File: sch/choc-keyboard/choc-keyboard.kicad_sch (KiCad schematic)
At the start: 1 part

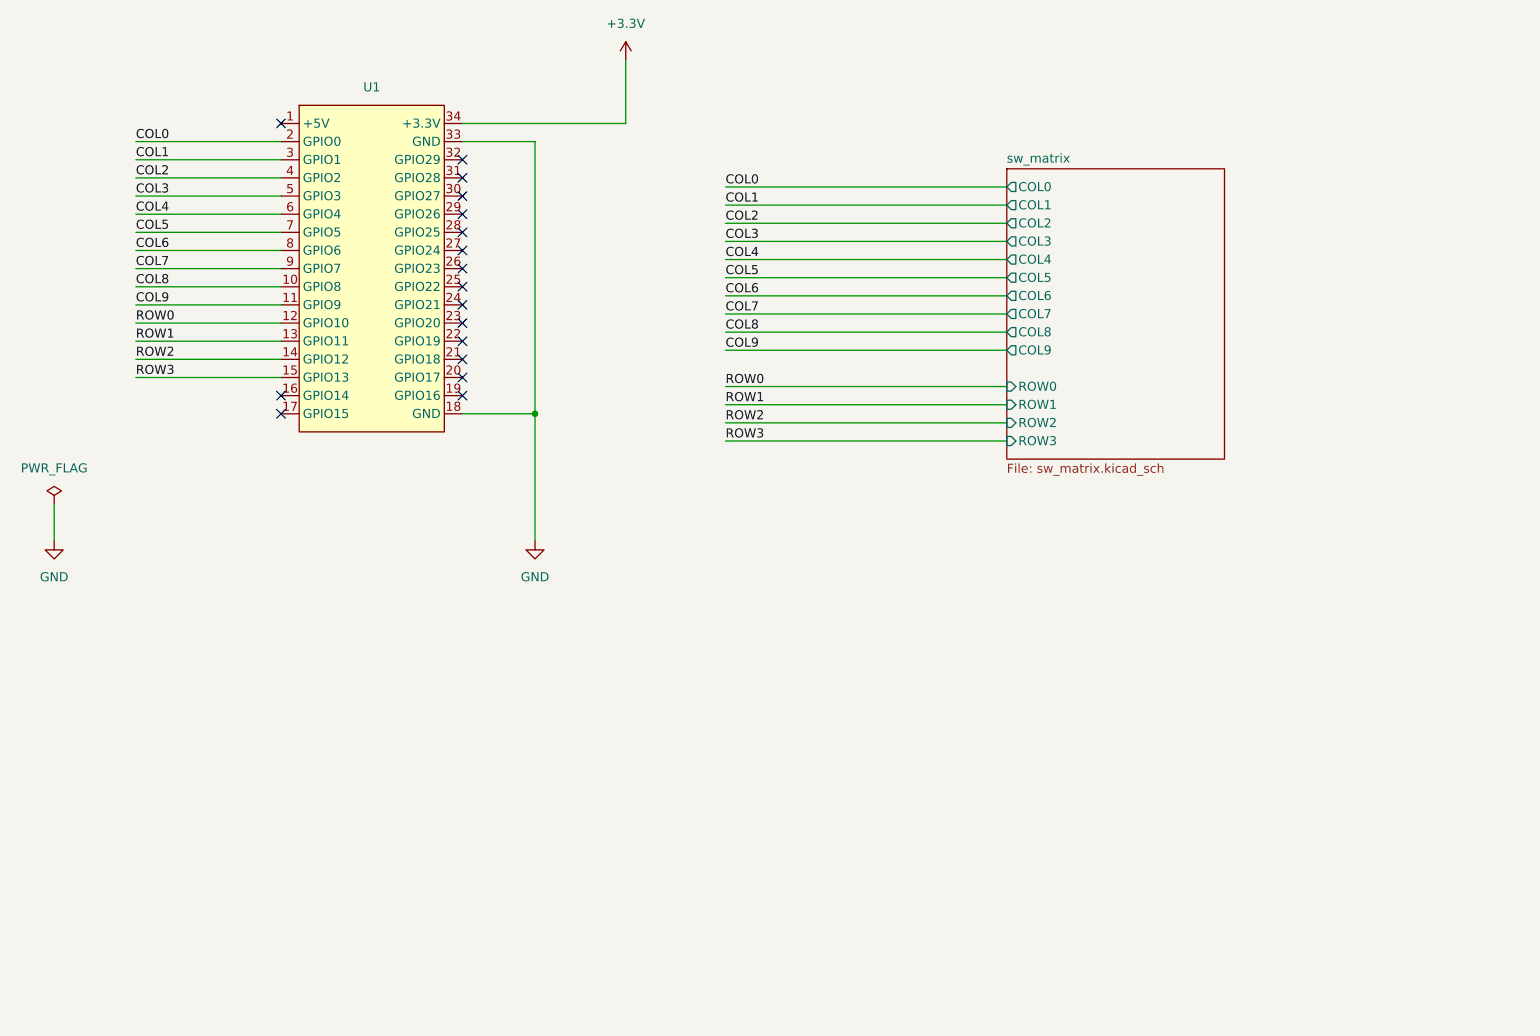
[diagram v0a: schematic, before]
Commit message: 配線しながらマイコンのピン配を検討中。
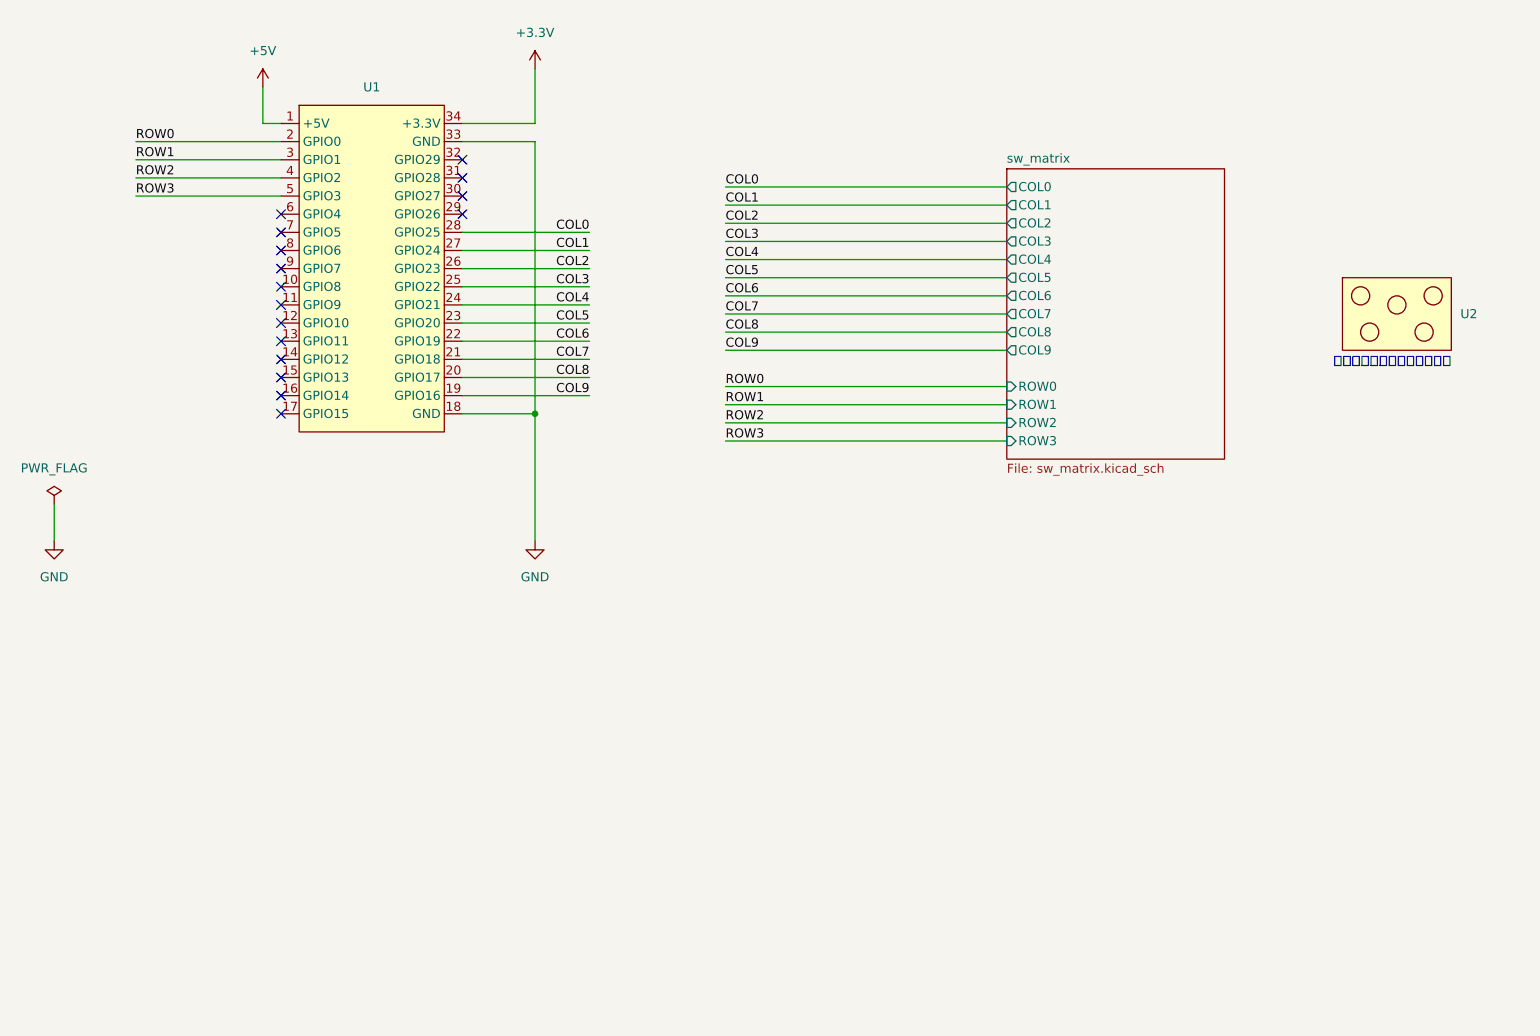
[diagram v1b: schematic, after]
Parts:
- added U2: ~, trackpoint:trackpoint_t400, symbol trackpoint:trackpoint_t400
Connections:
- net COL0: now also U1.28 (GPIO25); no longer U1.2 (GPIO0)
- net COL1: now also U1.27 (GPIO24); no longer U1.3 (GPIO1)
- net COL2: now also U1.26 (GPIO23); no longer U1.4 (GPIO2)
- net COL3: now also U1.25 (GPIO22); no longer U1.5 (GPIO3)
- net COL4: now also U1.24 (GPIO21); no longer U1.6 (GPIO4)
- net COL5: now also U1.23 (GPIO20); no longer U1.7 (GPIO5)
- net COL6: now also U1.22 (GPIO19); no longer U1.8 (GPIO6)
- net COL7: now also U1.21 (GPIO18); no longer U1.9 (GPIO7)
- net COL8: now also U1.20 (GPIO17); no longer U1.10 (GPIO8)
- net COL9: now also U1.19 (GPIO16); no longer U1.11 (GPIO9)
- net ROW0: now also U1.2 (GPIO0); no longer U1.12 (GPIO10)
- net ROW1: now also U1.3 (GPIO1); no longer U1.13 (GPIO11)
- net ROW2: now also U1.4 (GPIO2); no longer U1.14 (GPIO12)
- net ROW3: now also U1.5 (GPIO3); no longer U1.15 (GPIO13)
- net +5V: now reaches U1.1 (+5V)
- no-connect marks 17 -> 16
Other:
- note added: "トラックポイント取り付け穴"

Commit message: ネジ穴のぶん基板を大きくしました。
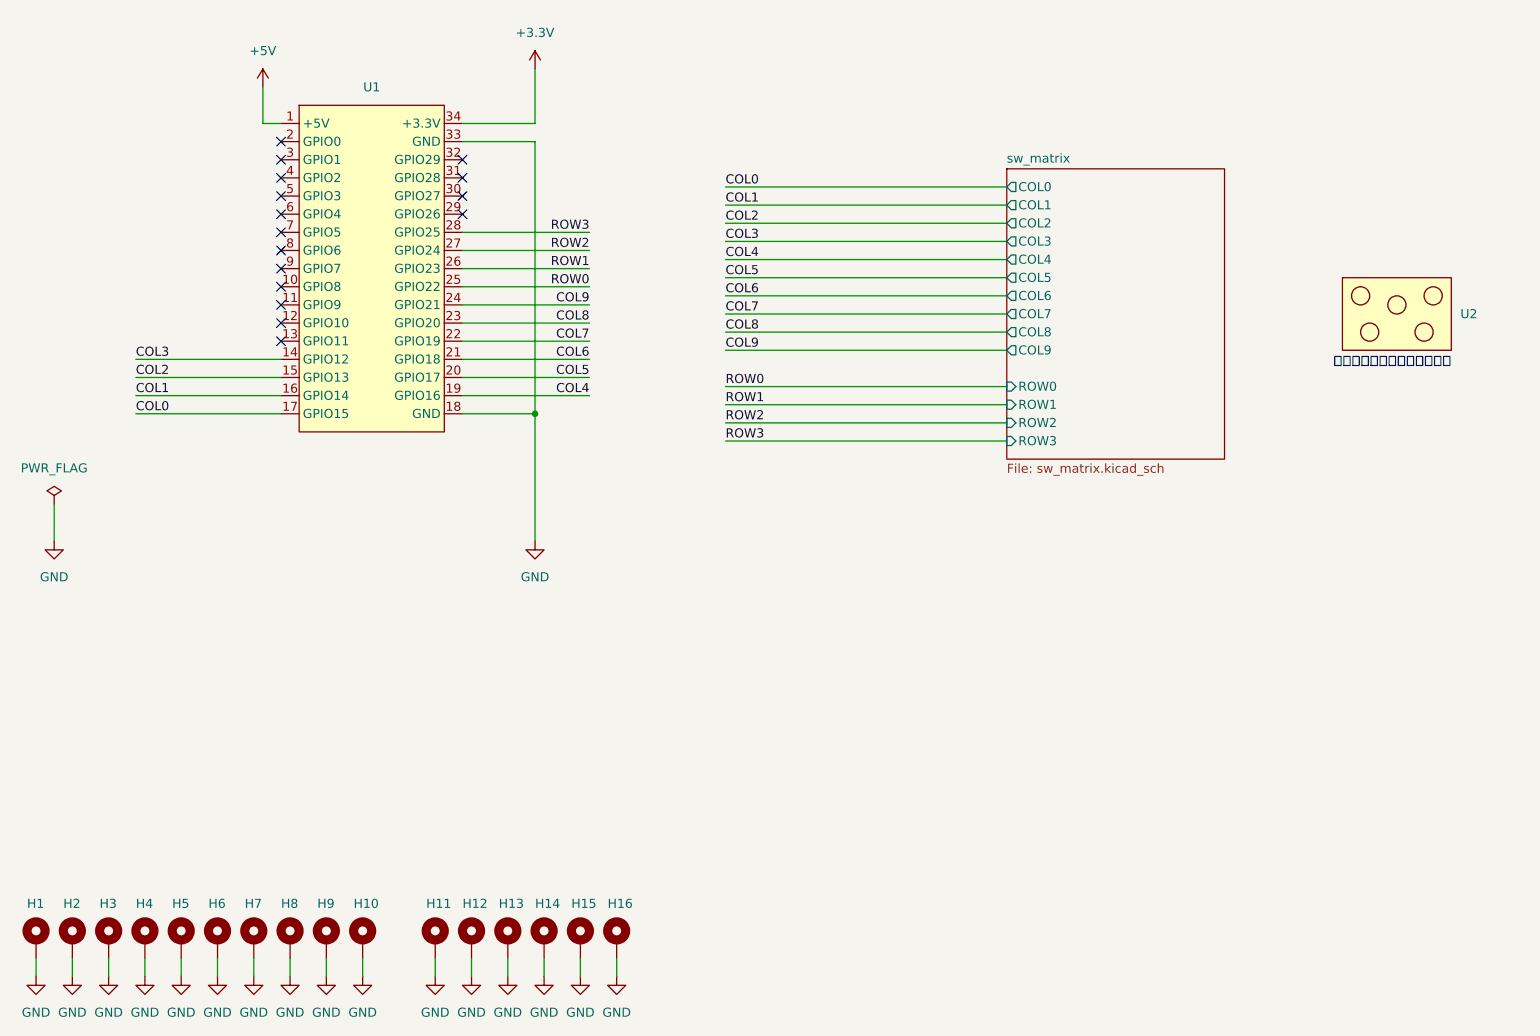
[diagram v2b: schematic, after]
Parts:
- added H1, H10, H11, H12, H13, H14, H15, H16, H2, H3, H4, H5, H6, H7, H8, H9: MountingHole_Pad, MountingHole:MountingHole_2.2mm_M2_Pad, symbol Mechanical:MountingHole_Pad
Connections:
- net COL0: now also U1.17 (GPIO15); no longer U1.28 (GPIO25)
- net COL1: now also U1.16 (GPIO14); no longer U1.27 (GPIO24)
- net COL2: now also U1.15 (GPIO13); no longer U1.26 (GPIO23)
- net COL3: now also U1.14 (GPIO12); no longer U1.25 (GPIO22)
- net COL4: now also U1.19 (GPIO16); no longer U1.24 (GPIO21)
- net COL5: now also U1.20 (GPIO17); no longer U1.23 (GPIO20)
- net COL6: now also U1.21 (GPIO18); no longer U1.22 (GPIO19)
- net COL7: now also U1.22 (GPIO19); no longer U1.21 (GPIO18)
- net COL8: now also U1.23 (GPIO20); no longer U1.20 (GPIO17)
- net COL9: now also U1.24 (GPIO21); no longer U1.19 (GPIO16)
- net GND: now also H1.1, H10.1, H11.1, H12.1, H13.1, H14.1, H15.1, H16.1, H2.1, H3.1, H4.1, H5.1, H6.1, H7.1, H8.1, H9.1
- net ROW0: now also U1.25 (GPIO22); no longer U1.2 (GPIO0)
- net ROW1: now also U1.26 (GPIO23); no longer U1.3 (GPIO1)
- net ROW2: now also U1.27 (GPIO24); no longer U1.4 (GPIO2)
- net ROW3: now also U1.28 (GPIO25); no longer U1.5 (GPIO3)

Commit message: キャラクタLCDを追加。
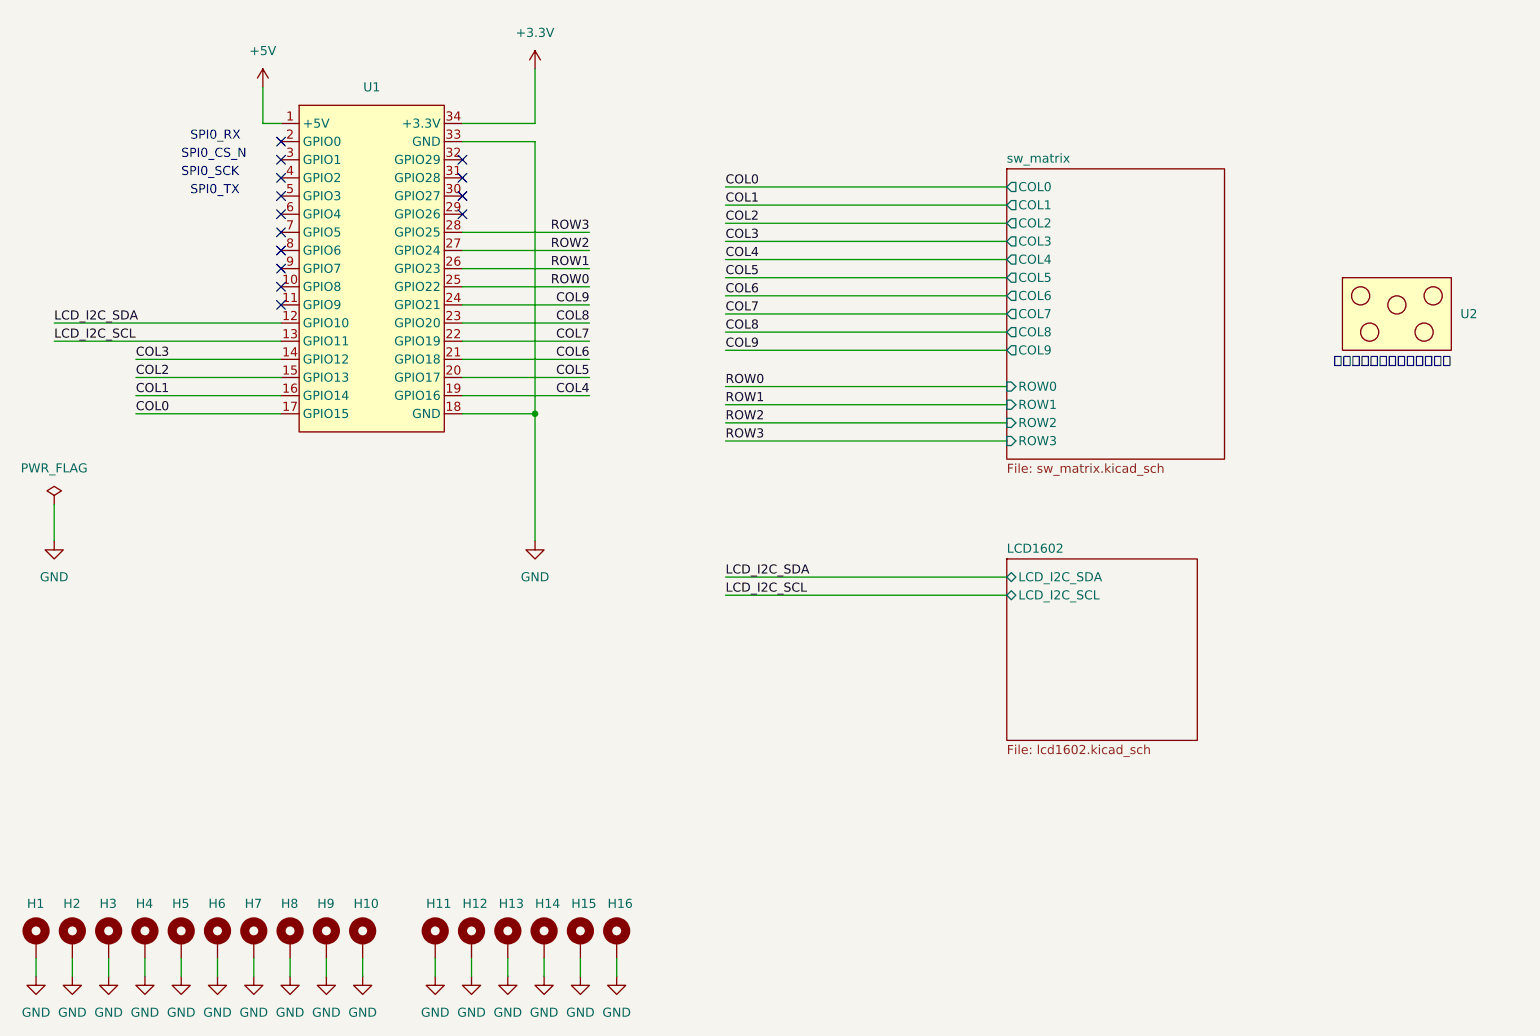
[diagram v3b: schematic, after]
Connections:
- net LCD_I2C_SDA: now reaches U1.12 (GPIO10)
- net LCD_I2C_SCL: now reaches U1.13 (GPIO11)
- no-connect marks 16 -> 14
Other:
- added sheet LCD1602 (lcd1602.kicad_sch)
- note added: "SPI0_CS_N"
- note added: "SPI0_RX"
- note added: "SPI0_SCK"
- note added: "SPI0_TX"
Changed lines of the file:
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@@
   (no_connect (at 55.88 74.93))
   (no_connect (at 81.28 57.15))
-  (no_connect (at 55.88 54.61))
   (no_connect (at 55.88 72.39))
   (no_connect (at 55.88 77.47))
   (no_connect (at 55.88 64.77))
-  (no_connect (at 55.88 80.01))
   (no_connect (at 55.88 69.85))
-  (no_connect (at 55.88 82.55))
   (no_connect (at 55.88 59.69))
   (no_connect (at 81.28 64.77))
   (no_connect (at 55.88 62.23))
+  (no_connect (at 55.88 54.61))
   (wire (pts (xy 118.11 60.96) (xy 157.48 60.96))
     (stroke (width 0) (type default))
@@
     (stroke (width 0) (type default))
   )
+  (wire (pts (xy 118.11 115.57) (xy 157.48 115.57))
+    (stroke (width 0) (type default))
+  )
   (wire (pts (xy 81.28 52.07) (xy 91.44 52.07))
     (stroke (width 0) (type default))
@@
     (stroke (width 0) (type default))
   )
+  (wire (pts (xy 118.11 118.11) (xy 157.48 118.11))
+    (stroke (width 0) (type default))
+  )
   (wire (pts (xy 81.28 72.39) (xy 99.06 72.39))
     (stroke (width 0) (type default))
@@
     (stroke (width 0) (type default))
   )
+  (wire (pts (xy 24.13 82.55) (xy 55.88 82.55))
+    (stroke (width 0) (type default))
+  )
   (wire (pts (xy 87.63 168.91) (xy 87.63 171.45))
     (stroke (width 0) (type default))
@@
     (stroke (width 0) (type default))
   )
+  (wire (pts (xy 24.13 80.01) (xy 55.88 80.01))
+    (stroke (width 0) (type default))
+  )
   (wire (pts (xy 118.11 83.82) (xy 157.48 83.82))
     (stroke (width 0) (type default))
@@
   )
   (text "トラックポイント取り付け穴" (at 203.2 86.36 0)
+    (effects (font (size 1.27 1.27)) (justify left bottom))
+  )
+  (text "SPI0_TX" (at 43.18 62.23 0)
+    (effects (font (size 1.27 1.27)) (justify left bottom))
+  )
+  (text "SPI0_SCK" (at 41.91 59.69 0)
+    (effects (font (size 1.27 1.27)) (justify left bottom))
+  )
+  (text "SPI0_RX" (at 43.18 54.61 0)
+    (effects (font (size 1.27 1.27)) (justify left bottom))
+  )
+  (text "SPI0_CS_N" (at 41.91 57.15 0)
     (effects (font (size 1.27 1.27)) (justify left bottom))
   )
@@
     (effects (font (size 1.27 1.27)) (justify right bottom))
   )
+  (label "LCD_I2C_SDA" (at 24.13 80.01 0) (fields_autoplaced)
+    (effects (font (size 1.27 1.27)) (justify left bottom))
+  )
+  (label "LCD_I2C_SCL" (at 24.13 82.55 0) (fields_autoplaced)
+    (effects (font (size 1.27 1.27)) (justify left bottom))
+  )
   (label "ROW3" (at 99.06 67.31 180) (fields_autoplaced)
     (effects (font (size 1.27 1.27)) (justify right bottom))
@@
   )
   (label "COL4" (at 118.11 71.12 0) (fields_autoplaced)
+    (effects (font (size 1.27 1.27)) (justify left bottom))
+  )
+  (label "LCD_I2C_SCL" (at 118.11 118.11 0) (fields_autoplaced)
+    (effects (font (size 1.27 1.27)) (justify left bottom))
+  )
+  (label "LCD_I2C_SDA" (at 118.11 115.57 0) (fields_autoplaced)
     (effects (font (size 1.27 1.27)) (justify left bottom))
   )
@@
       )
     )
+  )
+  (sheet (at 157.48 113.03) (size 26.67 25.4) (fields_autoplaced)
+    (stroke (width 0.1524) (type solid))
+    (fill (color 0 0 0 0.0000))
+    (property "Sheetname" "LCD1602" (at 157.48 112.3184 0)
+      (effects (font (size 1.27 1.27)) (justify left bottom))
+    )
+    (property "Sheetfile" "lcd1602.kicad_sch" (at 157.48 139.0146 0)
+      (effects (font (size 1.27 1.27)) (justify left top))
+    )
+    (pin "LCD_I2C_SCL" bidirectional (at 157.48 118.11 180)
+      (effects (font (size 1.27 1.27)) (justify left))
+    )
+    (pin "LCD_I2C_SDA" bidirectional (at 157.48 115.57 180)
+      (effects (font (size 1.27 1.27)) (justify left))
+    )
+    (instances
+      (project "choc-keyboard"
+        (path "/ab848e7f-81e1-4af5-91ec-8d4a44ffb559" (page "3"))
+      )
+    )
